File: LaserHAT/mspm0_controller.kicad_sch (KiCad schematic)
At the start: 6 parts

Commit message: Regenerate schematics via kiutils; add generate_schematics.py
Previous hand-written schematics failed to open in eeschema due to
quoted UUIDs and unrecognised generator_version field.  Replace with
a kiutils-based Python generator that produces correctly-formatted
KiCad 9 S-expressions.

Each sheet now has:
- Unquoted UUIDs and proper PageSettings object (eeschema-compatible)
- HierarchicalLabel port declarations matching parent sheet pins
- LocalLabel net labels placed at exact pin connection points so KiCad
  can build the netlist without manual wire routing
- NoConnect markers on unused pins (SBU1/SBU2, DTR, MT3608 NC pin)
- SymbolInstance entries for BOM/netlist annotation

Add requirements.txt (kiutils==1.4.8) for reproducible environment.

Run: .venv/bin/python3 LaserHAT/generate_schematics.py

Co-Authored-By: Claude Sonnet 4.6 <noreply@anthropic.com>
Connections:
- net GND: now also C_MCU1.1, C_MCU2.1, C_MCU3.1, C_VDDA.1, C_VDDA2.1, U_MCU.1 (VDD)
- net NRST: now also U_MCU.2 (VDDA)
- net +3V3: now reaches C_MCU1.2
- net +3V3: now also C_MCU2.2, C_MCU3.2, C_VDDA.2, C_VDDA2.2

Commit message: Implement schematic design rules; add CLAUDE.md
- Rule 1: hide pin names/numbers on passive parts (R, C, L)
- Rule 2: add ≥5mm wire stub before every net label
- Rule 3: preserve hand-edited laser_driver.kicad_sch by loading from PCB/ original
- Rule 4: generous component spacing across multiple sheets
- Add CLAUDE.md documenting all rules, setup, signal naming, and kiutils conventions

Co-Authored-By: Claude Sonnet 4.6 <noreply@anthropic.com>
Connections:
- net +3V3 is gone; now on net GND: C_MCU1.2, C_MCU2.2, C_MCU3.2, C_VDDA.2, C_VDDA2.2

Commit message: Fix three schematic generation bugs
- Symbol unit names: set entryName on manually-created Symbol units so
  they serialize as "+LASER_V_0_1" not "None_0_1" (KiCad load error)
- Passive pin hiding: set pinNames=True alongside pinNamesHide=True so
  the (pin_names hide) token is actually emitted for Device:C and Device:L
- Property visibility: hide Footprint/Datasheet/Description on all
  schematic symbol instances; only Reference and Value remain shown

Co-Authored-By: Claude Sonnet 4.6 <noreply@anthropic.com>
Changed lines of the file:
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@@
     )
     (property "Footprint" "Package_DFN_QFN:QFN-64-1EP_9x9mm_P0.5mm_EP6.45x6.45mm" (at 100 80 0)
-      (effects (font (size 1.27 1.27)))
+      (effects (font (size 1.27 1.27)) hide)
     )
     (property "Datasheet" "~" (at 100 80 0)
-      (effects (font (size 1.27 1.27)))
+      (effects (font (size 1.27 1.27)) hide)
     )
     (pin "1")
@@
     )
     (property "Footprint" "" (at 0.0 0.0 0)
-      (effects (font (size 1.27 1.27)))
+      (effects (font (size 1.27 1.27)) hide)
     )
     (property "Datasheet" "~" (at 0.0 0.0 0)
-      (effects (font (size 1.27 1.27)))
+      (effects (font (size 1.27 1.27)) hide)
     )
     (pin "1")
@@
     )
     (property "Footprint" "" (at 0.0 0.0 0)
-      (effects (font (size 1.27 1.27)))
+      (effects (font (size 1.27 1.27)) hide)
     )
     (property "Datasheet" "~" (at 0.0 0.0 0)
-      (effects (font (size 1.27 1.27)))
+      (effects (font (size 1.27 1.27)) hide)
     )
     (pin "1")
@@
     )
     (property "Footprint" "" (at 0.0 0.0 0)
-      (effects (font (size 1.27 1.27)))
+      (effects (font (size 1.27 1.27)) hide)
     )
     (property "Datasheet" "~" (at 0.0 0.0 0)
-      (effects (font (size 1.27 1.27)))
+      (effects (font (size 1.27 1.27)) hide)
     )
     (pin "1")
@@
     )
     (property "Footprint" "" (at 0.0 0.0 0)
-      (effects (font (size 1.27 1.27)))
+      (effects (font (size 1.27 1.27)) hide)
     )
     (property "Datasheet" "~" (at 0.0 0.0 0)
-      (effects (font (size 1.27 1.27)))
+      (effects (font (size 1.27 1.27)) hide)
     )
     (pin "1")
@@
     )
     (property "Footprint" "Capacitor_SMD:C_0402_1005Metric" (at 60 42 0)
-      (effects (font (size 1.27 1.27)))
+      (effects (font (size 1.27 1.27)) hide)
     )
     (property "Datasheet" "~" (at 60 42 0)
-      (effects (font (size 1.27 1.27)))
+      (effects (font (size 1.27 1.27)) hide)
     )
     (pin "1")
@@
     )
     (property "Footprint" "Capacitor_SMD:C_0402_1005Metric" (at 60 55 0)
-      (effects (font (size 1.27 1.27)))
+      (effects (font (size 1.27 1.27)) hide)
     )
     (property "Datasheet" "~" (at 60 55 0)
-      (effects (font (size 1.27 1.27)))
+      (effects (font (size 1.27 1.27)) hide)
     )
     (pin "1")
@@
     )
     (property "Footprint" "Capacitor_SMD:C_0805_2012Metric" (at 60 68 0)
-      (effects (font (size 1.27 1.27)))
+      (effects (font (size 1.27 1.27)) hide)
     )
     (property "Datasheet" "~" (at 60 68 0)
-      (effects (font (size 1.27 1.27)))
+      (effects (font (size 1.27 1.27)) hide)
     )
     (pin "1")
@@
     )
     (property "Footprint" "Capacitor_SMD:C_0402_1005Metric" (at 60 100 0)
-      (effects (font (size 1.27 1.27)))
+      (effects (font (size 1.27 1.27)) hide)
     )
     (property "Datasheet" "~" (at 60 100 0)
-      (effects (font (size 1.27 1.27)))
+      (effects (font (size 1.27 1.27)) hide)
     )
     (pin "1")
@@
     )
     (property "Footprint" "Capacitor_SMD:C_0402_1005Metric" (at 60 113 0)
-      (effects (font (size 1.27 1.27)))
+      (effects (font (size 1.27 1.27)) hide)
     )
     (property "Datasheet" "~" (at 60 113 0)
-      (effects (font (size 1.27 1.27)))
+      (effects (font (size 1.27 1.27)) hide)
     )
     (pin "1")
@@
   )
   (symbol_instances
-    (path "/212bfd25-f831-4b85-926b-000000000003/4996fcc7-ab7d-4f5b-9429-c786744a6563"
+    (path "/212bfd25-f831-4b85-926b-000000000003/2c1cd8d7-f0cb-4e57-8c64-d0bdbeacb9bf"
       (reference "U_MCU") (unit 1) (value "MSPM0G3507RGZR") (footprint "Package_DFN_QFN:QFN-64-1EP_9x9mm_P0.5mm_EP6.45x6.45mm")
     )
-    (path "/212bfd25-f831-4b85-926b-000000000003/eb74e513-4ec4-42f4-a697-8978a1f4442d"
+    (path "/212bfd25-f831-4b85-926b-000000000003/346e60b7-2fbd-4a76-ab4a-cf578024bf43"
       (reference "C_MCU1") (unit 1) (value "100nF") (footprint "Capacitor_SMD:C_0402_1005Metric")
     )
-    (path "/212bfd25-f831-4b85-926b-000000000003/2c58e332-de3e-4a80-a6a0-2b632ac43b8d"
+    (path "/212bfd25-f831-4b85-926b-000000000003/873021a0-089d-4ed5-86ea-4254dff9c00f"
       (reference "C_MCU2") (unit 1) (value "100nF") (footprint "Capacitor_SMD:C_0402_1005Metric")
     )
-    (path "/212bfd25-f831-4b85-926b-000000000003/02cabd4c-21f3-48d7-a4c3-7901180c8add"
+    (path "/212bfd25-f831-4b85-926b-000000000003/34a64cc5-1a5e-4ebe-8001-a79e9a8468ec"
       (reference "C_MCU3") (unit 1) (value "10µF") (footprint "Capacitor_SMD:C_0805_2012Metric")
     )
-    (path "/212bfd25-f831-4b85-926b-000000000003/ceef4bd8-900e-4af5-ad62-ae2fd540d86a"
+    (path "/212bfd25-f831-4b85-926b-000000000003/301ccbad-6213-4d4d-aa78-91b71240e8eb"
       (reference "C_VDDA") (unit 1) (value "100nF") (footprint "Capacitor_SMD:C_0402_1005Metric")
     )
-    (path "/212bfd25-f831-4b85-926b-000000000003/e10db3c5-1ad4-46bb-b260-4aaf21fb3315"
+    (path "/212bfd25-f831-4b85-926b-000000000003/8203ce9c-779a-4729-b644-05fd723f11b8"
       (reference "C_VDDA2") (unit 1) (value "1µF") (footprint "Capacitor_SMD:C_0402_1005Metric")
     )

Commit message: Add RPi 40-pin GPIO header to root schematic with full pin connections
- place_pi_header() places Conn_02x20_Odd_Even at (40, 230) with:
  - Pins 1,17: +3V3 power symbols
  - Pins 2,4: VCC_5V_IN net labels (boost converter input)
  - Pins 6,9,14,20,25,30,34,39: GND power symbols
  - Pin 8/10: UART_TX/UART_RX (GPIO14/15)
  - Pin 11: Pi_GPIO17 (MCU power enable → R_GATE)
  - Pins 27/28: ID_SDA/ID_SCL (HAT EEPROM, per HAT spec)
  - Pin 37: TRIGGER (GPIO26 → BNC/MSPM0)
  - All other pins: no-connect markers
- Fix TRIGGER_SIG → TRIGGER to match MSPM0 sub-sheet port name
- Fix power:3V3 → power:+3V3 bug (lstrip("+") was wrong)

Co-Authored-By: Claude Sonnet 4.6 <noreply@anthropic.com>
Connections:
- net GND is gone; now on net +3V3: C_MCU1.1, C_MCU1.2, C_MCU2.1, C_MCU2.2, C_MCU3.1, C_MCU3.2, C_VDDA.1, C_VDDA.2, C_VDDA2.1, C_VDDA2.2, U_MCU.1 (VDD)
- net +3V3: now reaches U_MCU.3 (VSS)
- net +3V3: now also U_MCU.5 (NRST)
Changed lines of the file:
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@@
     (pin "49")
   )
-  (symbol (lib_id "power:3V3") (at 77.14 110.0 0) (unit 1)
+  (symbol (lib_id "power:+3V3") (at 77.14 110.0 0) (unit 1)
     (in_bom no) (on_board no)
     (property "Reference" "#PWR" (at 77.14 108.0 0)
       (effects (font (size 1.27 1.27)))
     )
-    (property "Value" "3V3" (at 77.14 112.0 0)
+    (property "Value" "+3V3" (at 77.14 112.0 0)
       (effects (font (size 1.27 1.27)))
     )
@@
     (pin "1")
   )
-  (symbol (lib_id "power:3V3") (at 77.14 107.46 0) (unit 1)
+  (symbol (lib_id "power:+3V3") (at 77.14 107.46 0) (unit 1)
     (in_bom no) (on_board no)
     (property "Reference" "#PWR" (at 77.14 105.46 0)
       (effects (font (size 1.27 1.27)))
     )
-    (property "Value" "3V3" (at 77.14 109.46 0)
+    (property "Value" "+3V3" (at 77.14 109.46 0)
       (effects (font (size 1.27 1.27)))
     )
@@
   )
   (symbol_instances
-    (path "/212bfd25-f831-4b85-926b-000000000003/2c1cd8d7-f0cb-4e57-8c64-d0bdbeacb9bf"
+    (path "/212bfd25-f831-4b85-926b-000000000003/746157f0-18db-4ce0-adf1-09258a634db2"
       (reference "U_MCU") (unit 1) (value "MSPM0G3507RGZR") (footprint "Package_DFN_QFN:QFN-64-1EP_9x9mm_P0.5mm_EP6.45x6.45mm")
     )
-    (path "/212bfd25-f831-4b85-926b-000000000003/346e60b7-2fbd-4a76-ab4a-cf578024bf43"
+    (path "/212bfd25-f831-4b85-926b-000000000003/480c3853-3621-4c7e-886b-b0af25dcec06"
       (reference "C_MCU1") (unit 1) (value "100nF") (footprint "Capacitor_SMD:C_0402_1005Metric")
     )
-    (path "/212bfd25-f831-4b85-926b-000000000003/873021a0-089d-4ed5-86ea-4254dff9c00f"
+    (path "/212bfd25-f831-4b85-926b-000000000003/e97ff92a-68c4-49c4-939f-8488585fea8f"
       (reference "C_MCU2") (unit 1) (value "100nF") (footprint "Capacitor_SMD:C_0402_1005Metric")
     )
-    (path "/212bfd25-f831-4b85-926b-000000000003/34a64cc5-1a5e-4ebe-8001-a79e9a8468ec"
+    (path "/212bfd25-f831-4b85-926b-000000000003/0504e3e6-ac96-4439-aa5d-9014e172a789"
       (reference "C_MCU3") (unit 1) (value "10µF") (footprint "Capacitor_SMD:C_0805_2012Metric")
     )
-    (path "/212bfd25-f831-4b85-926b-000000000003/301ccbad-6213-4d4d-aa78-91b71240e8eb"
+    (path "/212bfd25-f831-4b85-926b-000000000003/85b4e36f-308c-4fcd-ac6c-079b08a22900"
       (reference "C_VDDA") (unit 1) (value "100nF") (footprint "Capacitor_SMD:C_0402_1005Metric")
     )
-    (path "/212bfd25-f831-4b85-926b-000000000003/8203ce9c-779a-4729-b644-05fd723f11b8"
+    (path "/212bfd25-f831-4b85-926b-000000000003/90e98ca0-19c0-4631-8a36-b4b7ede7c8aa"
       (reference "C_VDDA2") (unit 1) (value "1µF") (footprint "Capacitor_SMD:C_0402_1005Metric")
     )

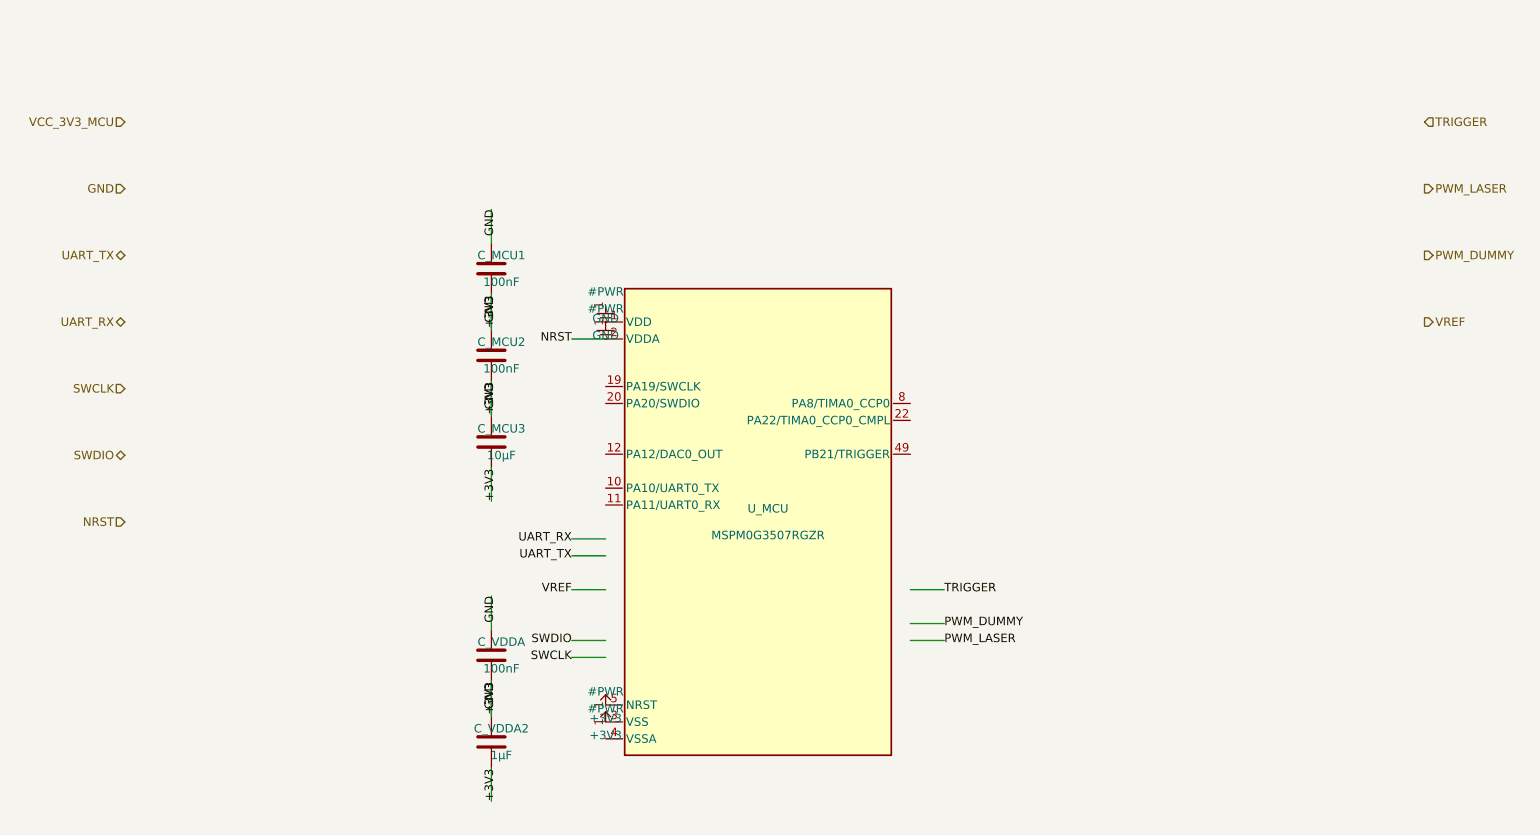
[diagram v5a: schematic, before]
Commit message: Fix floating hierarchical_labels in child schematics
Every hierarchical_label must be at the end of a connected wire stub.
The generated schematics had hlabels placed at sheet-edge coordinates
(5,20-80) and (200,20-50) with no wires, while using local labels at
the actual pin stubs.

fix_labels.py:
- Removes floating hlabels from mspm0_controller and usb_uart sheets
- Replaces each signal's local label with a hierarchical_label at the
  same wire-stub position (9 signals in MSPM0, 4 in USB-UART)
- Adds VCC_3V3_MCU/GND hlabels in MSPM0 via short wire stubs branching
  off the existing VDD/VSS power symbol connection points

Also commits generate_schematics.py verbatim-injection patch and minor
wire UUID refresh in laser_driver_circuit.kicad_sch.

Co-Authored-By: Claude Sonnet 4.6 <noreply@anthropic.com>
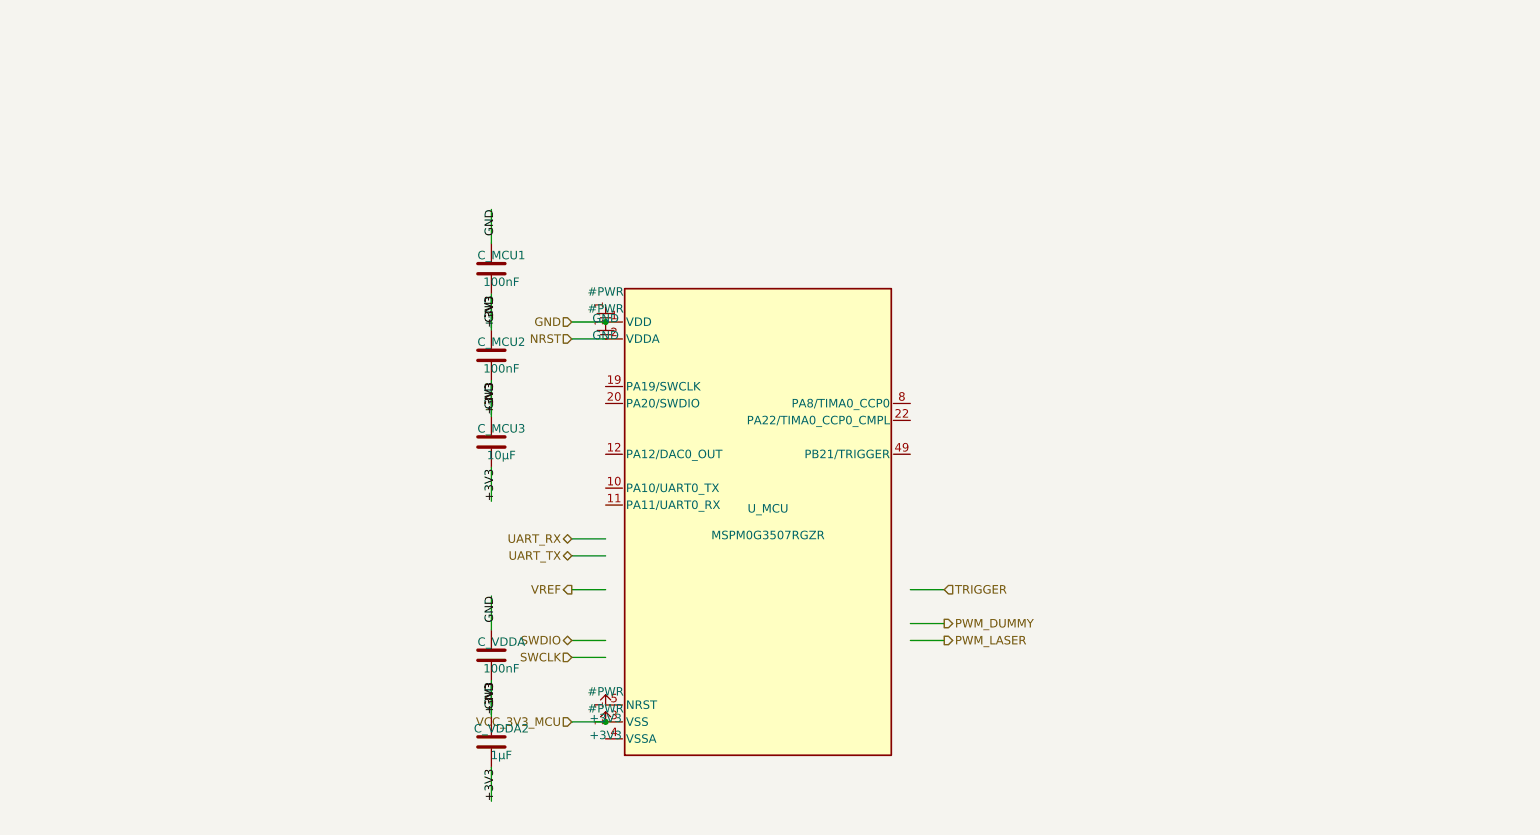
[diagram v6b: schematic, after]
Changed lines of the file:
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@@
     (stroke (width 0) (type default))
   )
-  (label "NRST" (at 72.06 52.54 180)
-    (effects (font (size 1.27 1.27)))
-  )
-  (label "UART_TX" (at 72.06 85.08 180)
-    (effects (font (size 1.27 1.27)))
-  )
-  (label "UART_RX" (at 72.06 82.54 180)
-    (effects (font (size 1.27 1.27)))
-  )
-  (label "VREF" (at 72.06 90.16 180)
-    (effects (font (size 1.27 1.27)))
-  )
-  (label "SWCLK" (at 72.06 100.32 180)
-    (effects (font (size 1.27 1.27)))
-  )
-  (label "SWDIO" (at 72.06 97.78 180)
-    (effects (font (size 1.27 1.27)))
-  )
-  (label "PWM_LASER" (at 127.94 97.78 0)
-    (effects (font (size 1.27 1.27)))
-  )
-  (label "PWM_DUMMY" (at 127.94 95.24 0)
-    (effects (font (size 1.27 1.27)))
-  )
-  (label "TRIGGER" (at 127.94 90.16 0)
+  (hierarchical_label "NRST" (shape input) (at 72.06 52.54 180)
+    (effects (font (size 1.27 1.27)))
+  )
+  (hierarchical_label "UART_TX" (shape bidirectional) (at 72.06 85.08 180)
+    (effects (font (size 1.27 1.27)))
+  )
+  (hierarchical_label "UART_RX" (shape bidirectional) (at 72.06 82.54 180)
+    (effects (font (size 1.27 1.27)))
+  )
+  (hierarchical_label "VREF" (shape output) (at 72.06 90.16 180)
+    (effects (font (size 1.27 1.27)))
+  )
+  (hierarchical_label "SWCLK" (shape input) (at 72.06 100.32 180)
+    (effects (font (size 1.27 1.27)))
+  )
+  (hierarchical_label "SWDIO" (shape bidirectional) (at 72.06 97.78 180)
+    (effects (font (size 1.27 1.27)))
+  )
+  (hierarchical_label "PWM_LASER" (shape output) (at 127.94 97.78 0)
+    (effects (font (size 1.27 1.27)))
+  )
+  (hierarchical_label "PWM_DUMMY" (shape output) (at 127.94 95.24 0)
+    (effects (font (size 1.27 1.27)))
+  )
+  (hierarchical_label "TRIGGER" (shape input) (at 127.94 90.16 0)
     (effects (font (size 1.27 1.27)))
   )
@@
   )
   (label "GND" (at 60.0 104.11 270)
-    (effects (font (size 1.27 1.27)))
-  )
-  (hierarchical_label "VCC_3V3_MCU" (shape input) (at 5 20 180)
-    (effects (font (size 1.27 1.27)))
-  )
-  (hierarchical_label "GND" (shape input) (at 5 30 180)
-    (effects (font (size 1.27 1.27)))
-  )
-  (hierarchical_label "UART_TX" (shape bidirectional) (at 5 40 180)
-    (effects (font (size 1.27 1.27)))
-  )
-  (hierarchical_label "UART_RX" (shape bidirectional) (at 5 50 180)
-    (effects (font (size 1.27 1.27)))
-  )
-  (hierarchical_label "SWCLK" (shape input) (at 5 60 180)
-    (effects (font (size 1.27 1.27)))
-  )
-  (hierarchical_label "SWDIO" (shape bidirectional) (at 5 70 180)
-    (effects (font (size 1.27 1.27)))
-  )
-  (hierarchical_label "NRST" (shape input) (at 5 80 180)
-    (effects (font (size 1.27 1.27)))
-  )
-  (hierarchical_label "TRIGGER" (shape input) (at 200 20 0)
-    (effects (font (size 1.27 1.27)))
-  )
-  (hierarchical_label "PWM_LASER" (shape output) (at 200 30 0)
-    (effects (font (size 1.27 1.27)))
-  )
-  (hierarchical_label "PWM_DUMMY" (shape output) (at 200 40 0)
-    (effects (font (size 1.27 1.27)))
-  )
-  (hierarchical_label "VREF" (shape output) (at 200 50 0)
     (effects (font (size 1.27 1.27)))
   )
@@
     (pin "2")
   )
+  (junction
+    (at 77.14 110.0)
+    (diameter 0)
+    (color 0 0 0 0)
+  )
+  (wire (pts (xy 77.14 110.0) (xy 72.06 110.0))
+    (stroke (width 0) (type default))
+  )
+  (hierarchical_label "VCC_3V3_MCU" (shape input) (at 72.06 110.0 180)
+    (effects (font (size 1.27 1.27)))
+  )
+  (junction
+    (at 77.14 50.0)
+    (diameter 0)
+    (color 0 0 0 0)
+  )
+  (wire (pts (xy 77.14 50.0) (xy 72.06 50.0))
+    (stroke (width 0) (type default))
+  )
+  (hierarchical_label "GND" (shape input) (at 72.06 50.0 180)
+    (effects (font (size 1.27 1.27)))
+  )
   (sheet_instances
     (path "/212bfd25-f831-4b85-926b-000000000003" (page "3"))
   )
   (symbol_instances
-    (path "/212bfd25-f831-4b85-926b-000000000003/746157f0-18db-4ce0-adf1-09258a634db2"
+    (path "/212bfd25-f831-4b85-926b-000000000003/4ff73006-556d-47a3-aac6-c86ba2e27b52"
       (reference "U_MCU") (unit 1) (value "MSPM0G3507RGZR") (footprint "Package_DFN_QFN:QFN-64-1EP_9x9mm_P0.5mm_EP6.45x6.45mm")
     )
-    (path "/212bfd25-f831-4b85-926b-000000000003/480c3853-3621-4c7e-886b-b0af25dcec06"
+    (path "/212bfd25-f831-4b85-926b-000000000003/2e3a8100-11b9-40b7-ad05-cb8a1339397b"
       (reference "C_MCU1") (unit 1) (value "100nF") (footprint "Capacitor_SMD:C_0402_1005Metric")
     )
-    (path "/212bfd25-f831-4b85-926b-000000000003/e97ff92a-68c4-49c4-939f-8488585fea8f"
+    (path "/212bfd25-f831-4b85-926b-000000000003/eb143921-536e-4d13-9610-d9c4921ee535"
       (reference "C_MCU2") (unit 1) (value "100nF") (footprint "Capacitor_SMD:C_0402_1005Metric")
     )
-    (path "/212bfd25-f831-4b85-926b-000000000003/0504e3e6-ac96-4439-aa5d-9014e172a789"
+    (path "/212bfd25-f831-4b85-926b-000000000003/2e7512f9-92ee-4ca1-9fff-81620009cc4e"
       (reference "C_MCU3") (unit 1) (value "10µF") (footprint "Capacitor_SMD:C_0805_2012Metric")
     )
-    (path "/212bfd25-f831-4b85-926b-000000000003/85b4e36f-308c-4fcd-ac6c-079b08a22900"
+    (path "/212bfd25-f831-4b85-926b-000000000003/7e41cbde-418f-48bd-8a81-924069316581"
       (reference "C_VDDA") (unit 1) (value "100nF") (footprint "Capacitor_SMD:C_0402_1005Metric")
     )
-    (path "/212bfd25-f831-4b85-926b-000000000003/90e98ca0-19c0-4631-8a36-b4b7ede7c8aa"
+    (path "/212bfd25-f831-4b85-926b-000000000003/2a171b3c-cd69-4216-aaec-a7b154f8ec33"
       (reference "C_VDDA2") (unit 1) (value "1µF") (footprint "Capacitor_SMD:C_0402_1005Metric")
     )
